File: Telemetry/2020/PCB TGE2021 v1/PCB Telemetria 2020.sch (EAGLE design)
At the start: 32 parts, among them IC1 INA240A1DR, IC2 MCP3221A6T-E_OTVAO, IC3 AZ1117IH-3.3TRG1, IC4 ACS758LCB-050B-PFF-T, IC5 ADS1115IDGSR

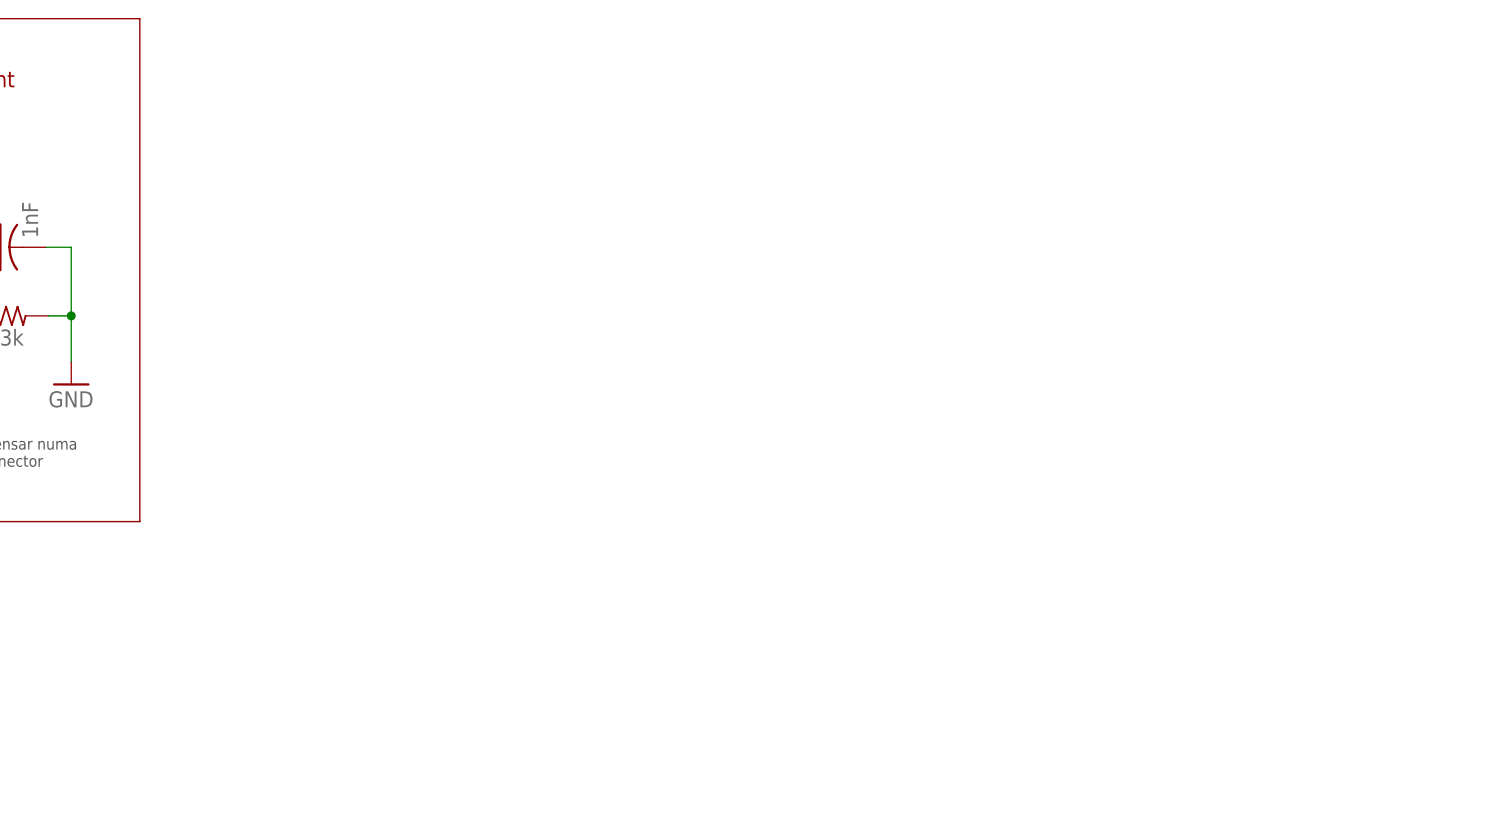
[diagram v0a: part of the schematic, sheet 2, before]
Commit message: adicionando novos circuitos a placa
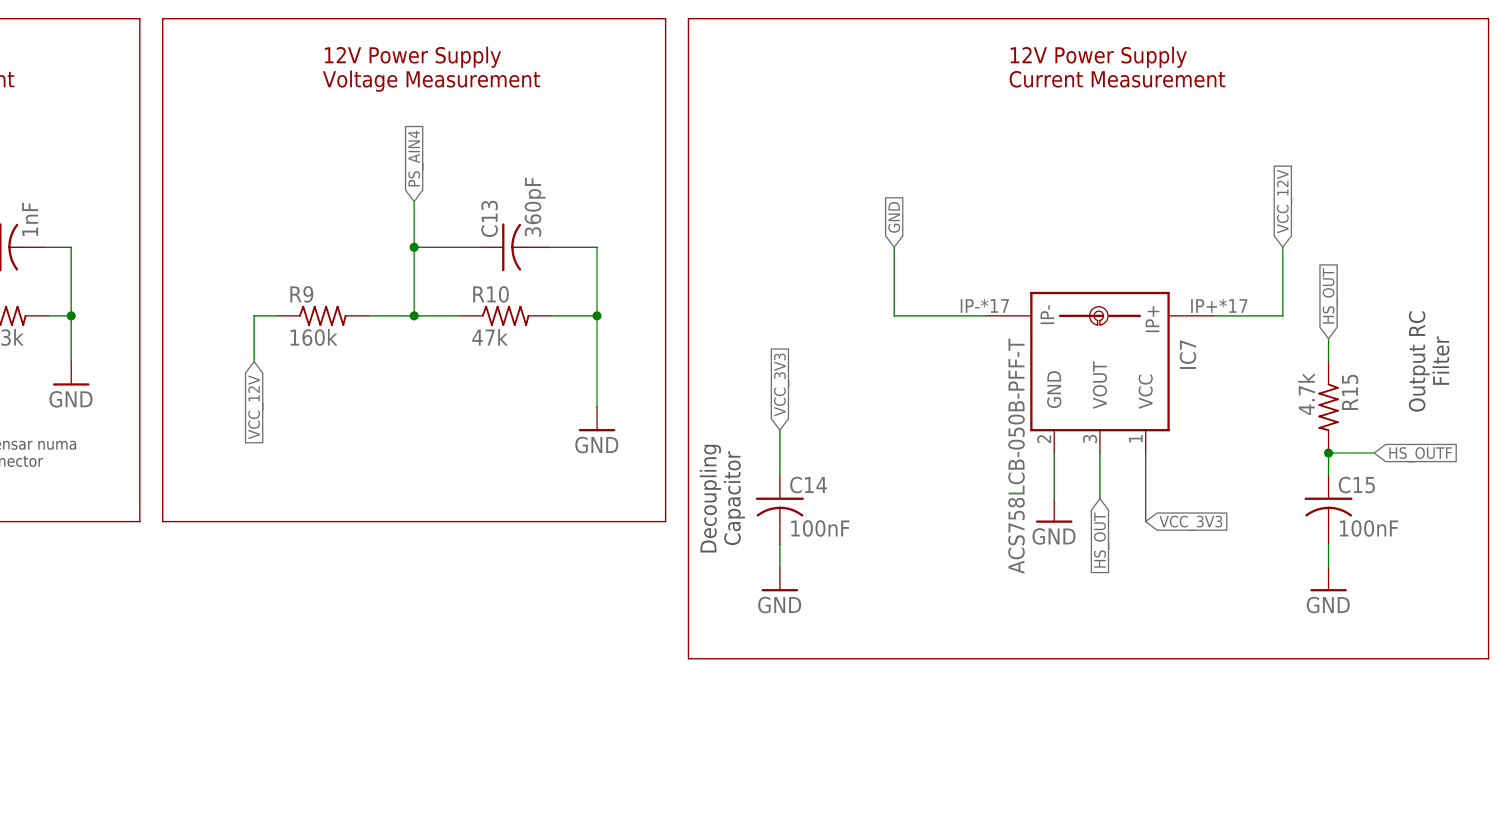
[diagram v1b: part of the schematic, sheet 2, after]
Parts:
- added C13: 360pF, rcl:C-USC0805
- added C14, C15: 100nF, rcl:C-USC0805
- added IC7: ACS758LCB-050B-PFF-T, allegro:ACS758LCB-050B-PFF-T
- added R10: 47k, rcl:R-US_R0805
- added R15: 4.7k, rcl:R-US_R0805
- added R9: 160k, rcl:R-US_R0805
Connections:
- new net HS_OUT: IC7.VOUT, R15.1
- new net HS_OUTF: C15.1, R15.2
- new net PS_AIN4: C13.1, R10.1, R9.2
- net GND: now also C13.2, C14.2, C15.2, IC7.GND, IC7.IP-, R10.2
- net VCC_12V: now also IC7.IP+, R9.1
- net VCC_3V3: now also C14.1, IC7.VCC
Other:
- note added: "12V Power Supply Current Measurement"
- note added: "12V Power Supply Voltage Measurement"
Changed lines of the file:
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@@
 <part name="C12" library="rcl" library_urn="urn:adsk.eagle:library:334" deviceset="C-US" device="C0805" package3d_urn="urn:adsk.eagle:package:23617/2"/>
 <part name="GND12" library="supply1" library_urn="urn:adsk.eagle:library:371" deviceset="GND" device=""/>
+<part name="R9" library="rcl" library_urn="urn:adsk.eagle:library:334" deviceset="R-US_" device="R0805" package3d_urn="urn:adsk.eagle:package:23553/2" value="160k"/>
+<part name="R10" library="rcl" library_urn="urn:adsk.eagle:library:334" deviceset="R-US_" device="R0805" package3d_urn="urn:adsk.eagle:package:23553/2" value="47k"/>
+<part name="GND13" library="supply1" library_urn="urn:adsk.eagle:library:371" deviceset="GND" device=""/>
+<part name="C13" library="rcl" library_urn="urn:adsk.eagle:library:334" deviceset="C-US" device="C0805" package3d_urn="urn:adsk.eagle:package:23617/2" value="360pF"/>
+<part name="IC7" library="allegro" library_urn="urn:adsk.eagle:library:93" deviceset="ACS758*" device="" package3d_urn="urn:adsk.eagle:package:3449/1" technology="LCB-050B-PFF-T"/>
+<part name="GND15" library="supply1" library_urn="urn:adsk.eagle:library:371" deviceset="GND" device=""/>
+<part name="C14" library="rcl" library_urn="urn:adsk.eagle:library:334" deviceset="C-US" device="C0805" package3d_urn="urn:adsk.eagle:package:23617/2" value="100nF"/>
+<part name="GND16" library="supply1" library_urn="urn:adsk.eagle:library:371" deviceset="GND" device=""/>
+<part name="C15" library="rcl" library_urn="urn:adsk.eagle:library:334" deviceset="C-US" device="C0805" package3d_urn="urn:adsk.eagle:package:23617/2" value="100nF"/>
+<part name="R15" library="rcl" library_urn="urn:adsk.eagle:library:334" deviceset="R-US_" device="R0805" package3d_urn="urn:adsk.eagle:package:23553/2" value="4.7k"/>
+<part name="GND17" library="supply1" library_urn="urn:adsk.eagle:library:371" deviceset="GND" device=""/>
 </parts>
 <sheets>
@@
 <text x="134.62" y="210.82" size="1.778" layer="94">PV Modules
 Voltage Measurement</text>
+<wire x1="233.68" y1="218.44" x2="233.68" y2="162.56" width="0.1524" layer="94"/>
+<text x="251.46" y="210.82" size="1.778" layer="94">12V Power Supply
+Voltage Measurement</text>
+<wire x1="289.56" y1="218.44" x2="233.68" y2="218.44" width="0.1524" layer="94"/>
+<wire x1="233.68" y1="162.56" x2="289.56" y2="162.56" width="0.1524" layer="94"/>
+<wire x1="289.56" y1="162.56" x2="289.56" y2="218.44" width="0.1524" layer="94"/>
+<wire x1="292.1" y1="218.44" x2="292.1" y2="147.32" width="0.1524" layer="94"/>
+<wire x1="292.1" y1="147.32" x2="381" y2="147.32" width="0.1524" layer="94"/>
+<wire x1="381" y1="147.32" x2="381" y2="218.44" width="0.1524" layer="94"/>
+<wire x1="381" y1="218.44" x2="292.1" y2="218.44" width="0.1524" layer="94"/>
+<text x="295.656" y="165.1" size="1.778" layer="97" rot="R90" align="center">Decoupling
+Capacitor</text>
+<text x="327.66" y="210.82" size="1.778" layer="94">12V Power Supply
+Current Measurement</text>
+<text x="374.396" y="180.34" size="1.778" layer="97" rot="R90" align="center">Output RC
+Filter</text>
 </plain>
 <instances>
@@
 <instance part="GND12" gate="1" x="165.1" y="177.8" smashed="yes">
 <attribute name="VALUE" x="162.56" y="175.26" size="1.778" layer="96"/>
+</instance>
+<instance part="R9" gate="G$1" x="251.46" y="185.42" smashed="yes">
+<attribute name="NAME" x="247.65" y="186.9186" size="1.778" layer="95"/>
+<attribute name="VALUE" x="247.65" y="182.118" size="1.778" layer="96"/>
+</instance>
+<instance part="R10" gate="G$1" x="271.78" y="185.42" smashed="yes">
+<attribute name="NAME" x="267.97" y="186.9186" size="1.778" layer="95"/>
+<attribute name="VALUE" x="267.97" y="182.118" size="1.778" layer="96"/>
+</instance>
+<instance part="GND13" gate="1" x="281.94" y="172.72" smashed="yes">
+<attribute name="VALUE" x="279.4" y="170.18" size="1.778" layer="96"/>
+</instance>
+<instance part="C13" gate="G$1" x="271.526" y="193.04" smashed="yes" rot="R90">
+<attribute name="NAME" x="270.891" y="194.056" size="1.778" layer="95" rot="R90"/>
+<attribute name="VALUE" x="275.717" y="194.056" size="1.778" layer="96" rot="R90"/>
+</instance>
+<instance part="IC7" gate="G$1" x="337.82" y="180.34" smashed="yes" rot="R270">
+<attribute name="NAME" x="346.71" y="182.88" size="1.778" layer="95" rot="R270"/>
+<attribute name="VALUE" x="327.66" y="182.88" size="1.778" layer="96" rot="R270"/>
+</instance>
+<instance part="GND15" gate="1" x="332.74" y="162.56" smashed="yes">
+<attribute name="VALUE" x="330.2" y="160.02" size="1.778" layer="96"/>
+</instance>
+<instance part="C14" gate="G$1" x="302.26" y="165.1" smashed="yes">
+<attribute name="NAME" x="303.276" y="165.735" size="1.778" layer="95"/>
+<attribute name="VALUE" x="303.276" y="160.909" size="1.778" layer="96"/>
+</instance>
+<instance part="GND16" gate="1" x="302.26" y="154.94" smashed="yes">
+<attribute name="VALUE" x="299.72" y="152.4" size="1.778" layer="96"/>
+</instance>
+<instance part="C15" gate="G$1" x="363.22" y="165.1" smashed="yes">
+<attribute name="NAME" x="364.236" y="165.735" size="1.778" layer="95"/>
+<attribute name="VALUE" x="364.236" y="160.909" size="1.778" layer="96"/>
+</instance>
+<instance part="R15" gate="G$1" x="363.22" y="175.26" smashed="yes" rot="R270">
+<attribute name="NAME" x="364.7186" y="179.07" size="1.778" layer="95" rot="R270"/>
+<attribute name="VALUE" x="359.918" y="179.07" size="1.778" layer="96" rot="R270"/>
+</instance>
+<instance part="GND17" gate="1" x="363.22" y="154.94" smashed="yes">
+<attribute name="VALUE" x="360.68" y="152.4" size="1.778" layer="96"/>
 </instance>
 </instances>
@@
 <pinref part="GND12" gate="1" pin="GND"/>
 </segment>
+<segment>
+<pinref part="R10" gate="G$1" pin="2"/>
+<pinref part="GND13" gate="1" pin="GND"/>
+<wire x1="276.86" y1="185.42" x2="281.94" y2="185.42" width="0.1524" layer="91"/>
+<wire x1="281.94" y1="185.42" x2="281.94" y2="175.26" width="0.1524" layer="91"/>
+<pinref part="C13" gate="G$1" pin="2"/>
+<wire x1="276.606" y1="193.04" x2="281.94" y2="193.04" width="0.1524" layer="91"/>
+<wire x1="281.94" y1="193.04" x2="281.94" y2="185.42" width="0.1524" layer="91"/>
+<junction x="281.94" y="185.42"/>
+</segment>
+<segment>
+<pinref part="IC7" gate="G$1" pin="GND"/>
+<pinref part="GND15" gate="1" pin="GND"/>
+<wire x1="332.74" y1="170.18" x2="332.74" y2="165.1" width="0.1524" layer="91"/>
+</segment>
+<segment>
+<pinref part="C14" gate="G$1" pin="2"/>
+<wire x1="302.26" y1="160.02" x2="302.26" y2="157.48" width="0.1524" layer="91"/>
+<pinref part="GND16" gate="1" pin="GND"/>
+</segment>
+<segment>
+<pinref part="GND17" gate="1" pin="GND"/>
+<pinref part="C15" gate="G$1" pin="2"/>
+<wire x1="363.22" y1="157.48" x2="363.22" y2="160.02" width="0.1524" layer="91"/>
+</segment>
+<segment>
+<pinref part="IC7" gate="G$1" pin="IP-"/>
+<wire x1="325.12" y1="185.42" x2="314.96" y2="185.42" width="0.1524" layer="91"/>
+<wire x1="314.96" y1="185.42" x2="314.96" y2="193.04" width="0.1524" layer="91"/>
+<label x="314.96" y="193.04" size="1.27" layer="95" rot="R90" xref="yes"/>
+</segment>
 </net>
 <net name="VCC_3V3" class="0">
@@
 <label x="96.52" y="198.12" size="1.27" layer="95" xref="yes"/>
 <wire x1="93.98" y1="198.12" x2="96.52" y2="198.12" width="0.1524" layer="91"/>
+</segment>
+<segment>
+<pinref part="IC7" gate="G$1" pin="VCC"/>
+<label x="342.9" y="162.56" size="1.27" layer="95" xref="yes"/>
+<wire x1="342.9" y1="162.56" x2="342.9" y2="170.18" width="0.1524" layer="91"/>
+</segment>
+<segment>
+<pinref part="C14" gate="G$1" pin="1"/>
+<wire x1="302.26" y1="167.64" x2="302.26" y2="172.72" width="0.1524" layer="91"/>
+<label x="302.26" y="172.72" size="1.27" layer="95" rot="R90" xref="yes"/>
 </segment>
 </net>
@@
 </segment>
 </net>
+<net name="PS_AIN4" class="0">
+<segment>
+<pinref part="R9" gate="G$1" pin="2"/>
+<pinref part="R10" gate="G$1" pin="1"/>
+<wire x1="256.54" y1="185.42" x2="261.62" y2="185.42" width="0.1524" layer="91"/>
+<junction x="261.62" y="185.42"/>
+<wire x1="261.62" y1="185.42" x2="266.7" y2="185.42" width="0.1524" layer="91"/>
+<wire x1="261.62" y1="185.42" x2="261.62" y2="193.04" width="0.1524" layer="91"/>
+<label x="261.62" y="198.12" size="1.27" layer="95" rot="R90" xref="yes"/>
+<pinref part="C13" gate="G$1" pin="1"/>
+<wire x1="261.62" y1="193.04" x2="261.62" y2="198.12" width="0.1524" layer="91"/>
+<wire x1="268.986" y1="193.04" x2="261.62" y2="193.04" width="0.1524" layer="91"/>
+<junction x="261.62" y="193.04"/>
+</segment>
+</net>
+<net name="VCC_12V" class="0">
+<segment>
+<pinref part="R9" gate="G$1" pin="1"/>
+<wire x1="246.38" y1="185.42" x2="243.84" y2="185.42" width="0.1524" layer="91"/>
+<wire x1="243.84" y1="185.42" x2="243.84" y2="180.34" width="0.1524" layer="91"/>
+<label x="243.84" y="180.34" size="1.27" layer="95" rot="R270" xref="yes"/>
+</segment>
+<segment>
+<pinref part="IC7" gate="G$1" pin="IP+"/>
+<wire x1="350.52" y1="185.42" x2="358.14" y2="185.42" width="0.1524" layer="91"/>
+<wire x1="358.14" y1="185.42" x2="358.14" y2="193.04" width="0.1524" layer="91"/>
+<label x="358.14" y="193.04" size="1.27" layer="95" rot="R90" xref="yes"/>
+</segment>
+</net>
+<net name="HS_OUT" class="0">
+<segment>
+<pinref part="IC7" gate="G$1" pin="VOUT"/>
+<wire x1="337.82" y1="170.18" x2="337.82" y2="165.1" width="0.1524" layer="91"/>
+<label x="337.82" y="165.1" size="1.27" layer="95" rot="R270" xref="yes"/>
+</segment>
+<segment>
+<pinref part="R15" gate="G$1" pin="1"/>
+<wire x1="363.22" y1="180.34" x2="363.22" y2="182.88" width="0.1524" layer="91"/>
+<label x="363.22" y="182.88" size="1.27" layer="95" rot="R90" xref="yes"/>
+</segment>
+</net>
+<net name="HS_OUTF" class="0">
+<segment>
+<pinref part="C15" gate="G$1" pin="1"/>
+<pinref part="R15" gate="G$1" pin="2"/>
+<wire x1="363.22" y1="167.64" x2="363.22" y2="170.18" width="0.1524" layer="91"/>
+<wire x1="363.22" y1="170.18" x2="368.3" y2="170.18" width="0.1524" layer="91"/>
+<junction x="363.22" y="170.18"/>
+<label x="368.3" y="170.18" size="1.27" layer="95" xref="yes"/>
+</segment>
+</net>
